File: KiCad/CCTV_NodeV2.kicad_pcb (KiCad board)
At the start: 2 copper layers, 100 x 80 mm, 9 parts, among them J1 SOLAR, J2 BATT, U1 CN3791, U2 BMS 1S, U3 MT3608, U4 ESP32-S3, U5 OV7670

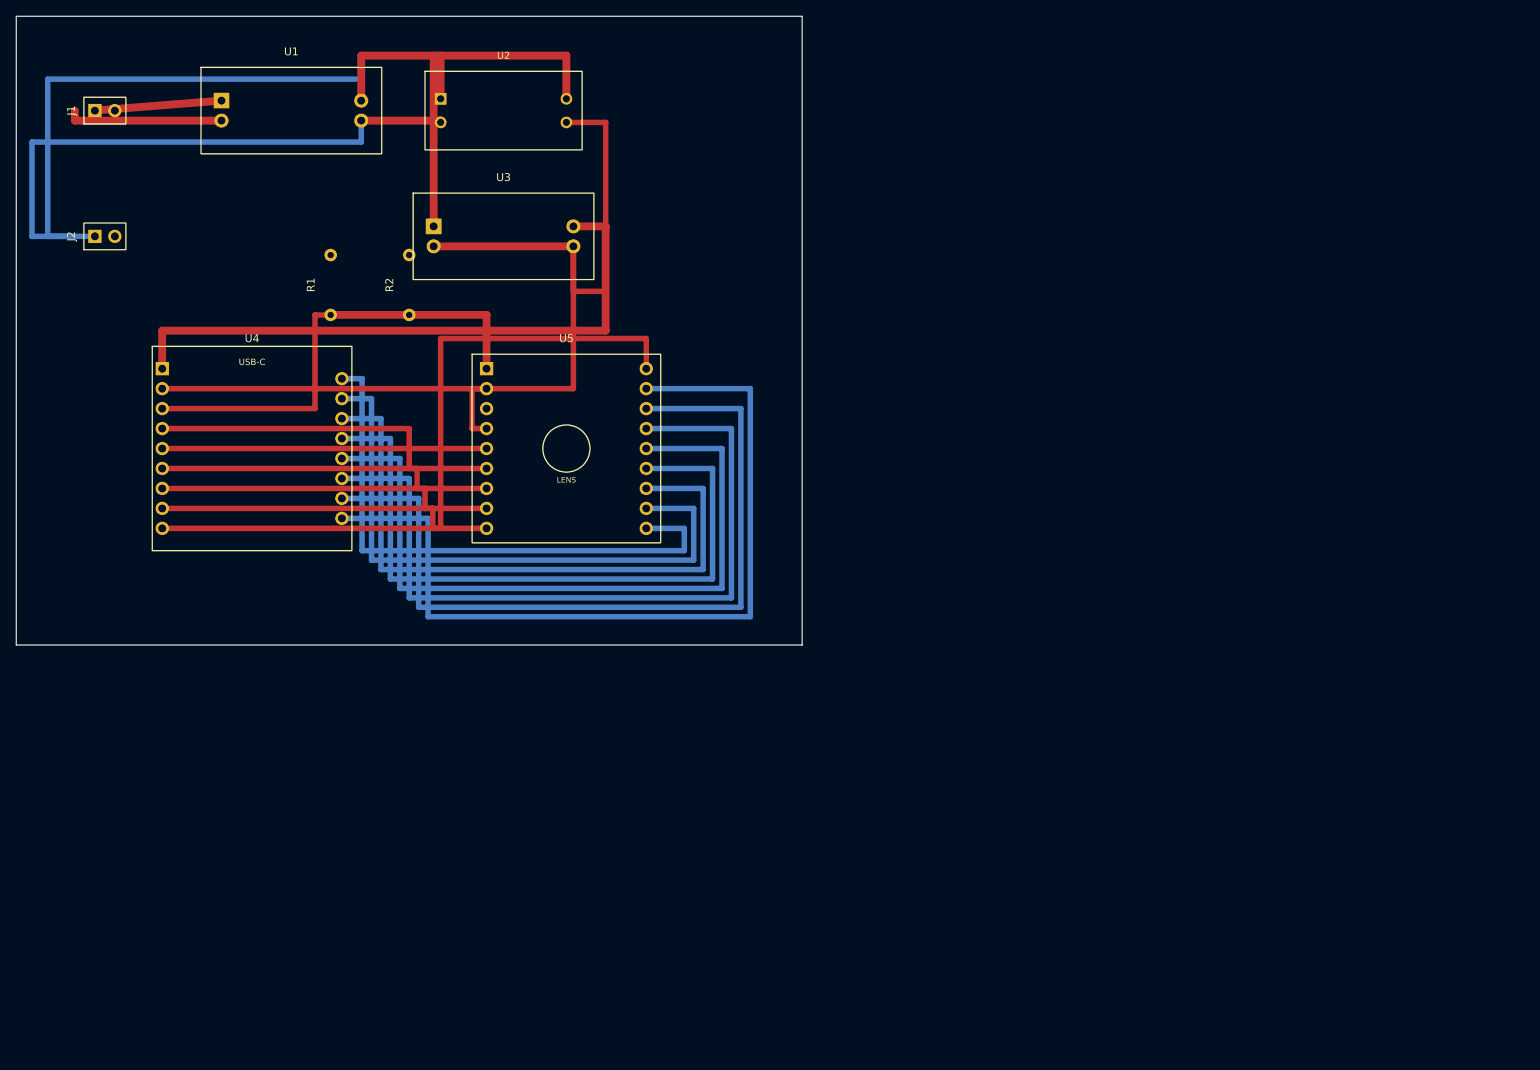
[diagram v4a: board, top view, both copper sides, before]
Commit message: Fix BMS → MT3608 power path: add P+ net, remove BATT+ bypass
The MT3608 boost converter was incorrectly connected directly to the
BATT+ net (raw battery positive), bypassing the 1S BMS protection.

Correct power flow (battery → BMS → MT3608 → 5V → ESP32):
  Battery J2 +  → BATT+  → BMS B+  (cell side, charging via CN3791)
  BMS P+ output → P+    → MT3608 IN+  (protected, load side)
  BMS P- output → PROT- → MT3608 IN-  (already correct)

Schematic (CCTV_NodeV2.kicad_sch):
- Removed stray BATT+ power flag at MT3608 IN+ (167.3, 64.92)
- Renamed net label at BMS P+ pin (142.7, 64.92): BATT+ → P+
- Renamed net label at MT3608 IN+ pin (167.3, 64.92): BATT+ → P+

PCB (CCTV_NodeV2.kicad_pcb):
- BMS pad 3 (P+ output): net BATT+ → P+
- MT3608 pad 1 (IN+):    net BATT+ → P+

The BMS over-discharge cutoff (DW01A ~2.4V trip) now actually
disconnects the MT3608 load via P-/PROT-. The P+ net is always the
same voltage as BATT+ when the BMS is conducting (1S BMS has no
MOSFET in the positive path), but labelling them separately in the
schematic makes the protection intent explicit.
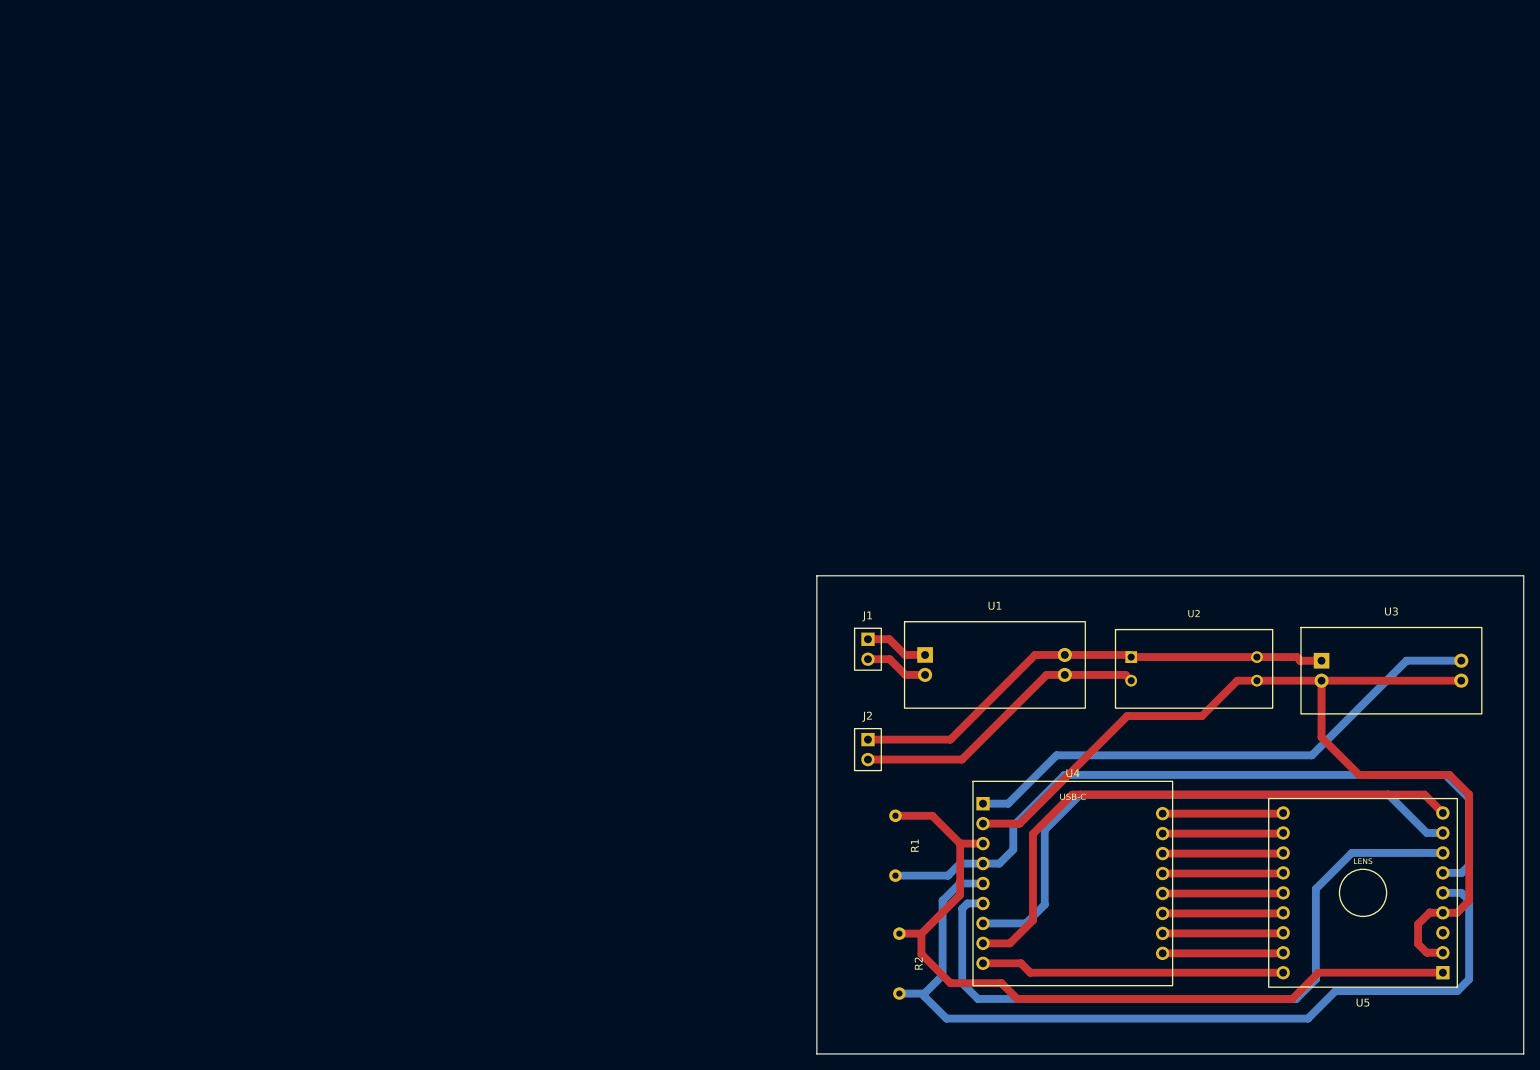
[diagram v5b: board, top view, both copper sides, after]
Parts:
- moved U3 125.8 mm to (175.0, 83.3)
- moved J1 119.2 mm to (108.4, 79.3), turned to 0 degrees
- moved U4 118.2 mm to (134.4, 110.3)
- moved J2 117.4 mm to (108.4, 92.0), turned to 0 degrees
- moved U5 116.1 mm to (171.4, 111.5), turned to 180 degrees
- moved U1 114.0 mm to (124.5, 82.5)
- moved U2 113.0 mm to (149.9, 83.0)
- moved R2 100.4 mm to (112.4, 116.7), turned to -90 degrees
- moved R1 96.1 mm to (111.9, 101.7), turned to -90 degrees
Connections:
- U2 pad 3: BATT+ -> P+
- U3 pad 1: BATT+ -> P+
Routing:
- net CAM_D7: track 106.7 -> 15.4 mm
- net CAM_D6: track 101.9 -> 15.4 mm
- net CAM_D5: track 97.1 -> 15.4 mm
- net CAM_D4: track 92.3 -> 15.4 mm
- net CAM_D3: track 87.5 -> 15.4 mm
- net BATT+: track 133.2 -> 62.6 mm
- net SIOC: track 41.3 -> 108.7 mm
- net CAM_D2: track 82.7 -> 15.4 mm
- net CAM_D1: track 77.9 -> 15.4 mm
- net CAM_D0: track 73.1 -> 15.4 mm
- net XCLK: track 89.6 -> 38.7 mm
- net SIOD: track 46.4 -> 93.6 mm
- net VSYNC: track 43.8 -> 88.8 mm
- net +3V3: track 60.0 -> 101.6 mm
- net BATT-: track 72.4 -> 38.3 mm
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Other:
- board size 100 x 80 mm -> 89.9 x 60.8 mm
